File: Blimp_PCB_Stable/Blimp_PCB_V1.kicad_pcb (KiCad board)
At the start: 2 copper layers, 109.9 x 62 mm, 26 parts, among them J1 S8B-PH-K-S, J2 S4B-XH-A

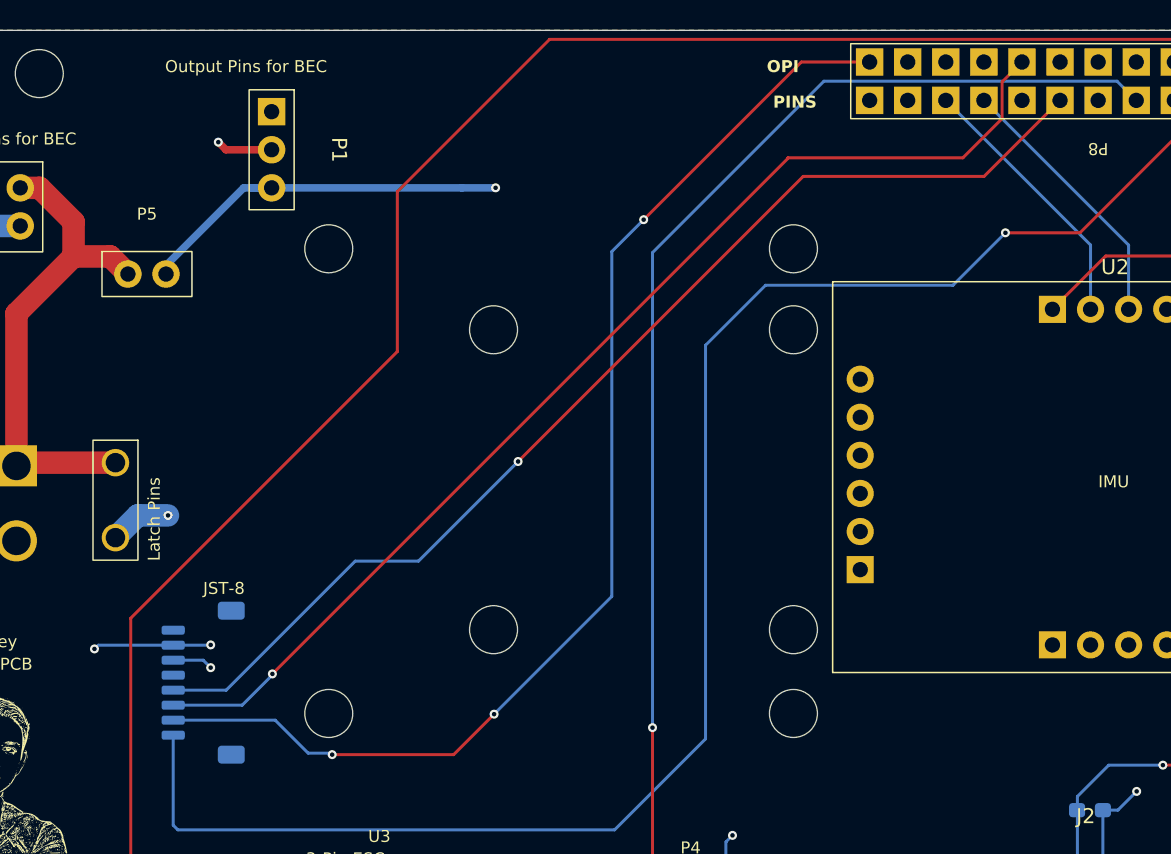
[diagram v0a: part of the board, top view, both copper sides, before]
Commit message: flip connector
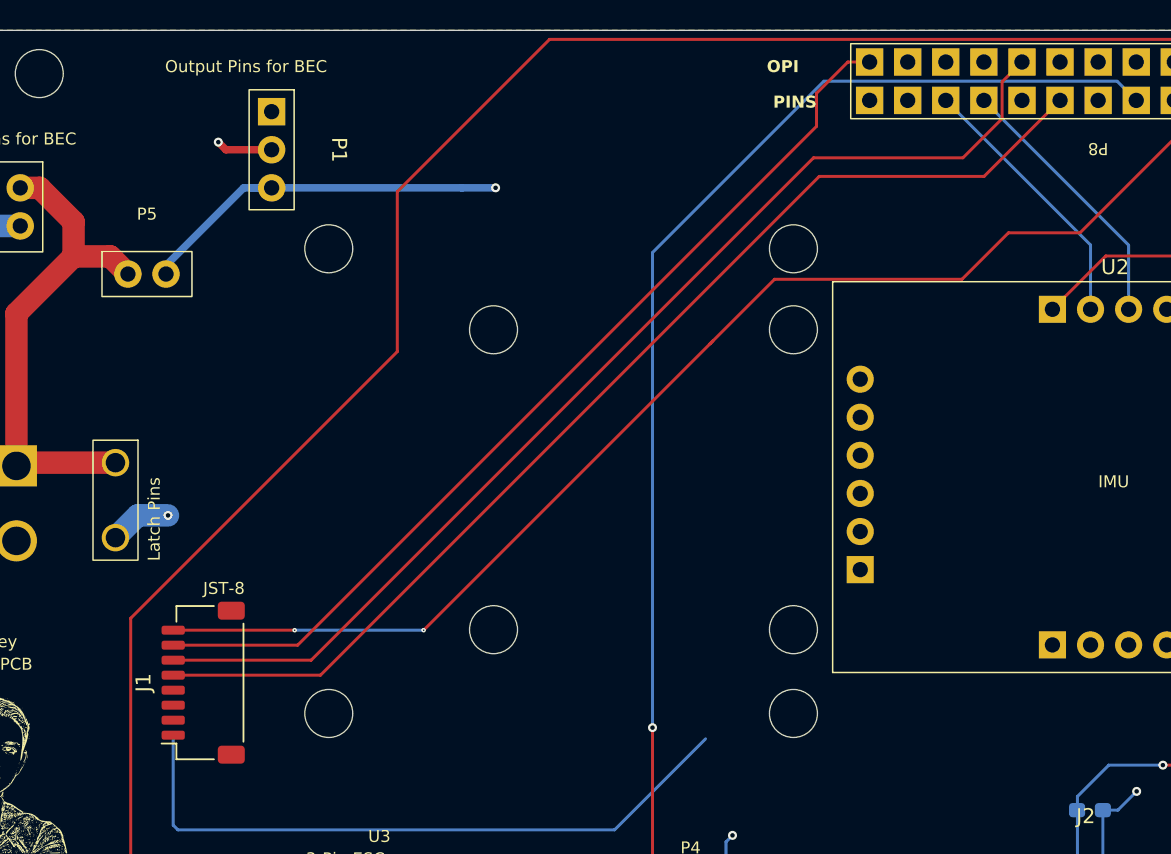
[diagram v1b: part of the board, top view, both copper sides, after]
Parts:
- J1: moved to F.Cu
- turned J1 to 90 degrees
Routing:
- net Net-(P8-PWM15): track 111.0 -> 128.4 mm, vias 1 -> 2
- net Net-(P8-PWM1): track 80.0 -> 63.9 mm, vias 3 -> 0
- net GND: track 71.4 -> 60.8 mm, vias 11 -> 8
- net Net-(P8-SCL.1): track 75.9 -> 74.6 mm, vias 1 -> 0
- net Net-(P8-CAN2_RX): track 75.4 -> 75.0 mm, vias 1 -> 0

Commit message: flip again
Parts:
- J1: moved to B.Cu
- turned J1 to -90 degrees
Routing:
- net Net-(P8-PWM15): track 128.4 -> 87.4 mm, vias 2 -> 1
- net Net-(P8-SDA.5): track 138.3 -> 127.3 mm
- net GND: track 60.8 -> 65.8 mm, vias 8 -> 10
- net Net-(P8-PWM1): track 63.9 -> 67.3 mm, vias 0 -> 3
- net Net-(P4-PWM): track 81.7 -> 85.2 mm
- net Net-(P8-SCL.1): track 74.6 -> 77.7 mm, vias 0 -> 1
- net Net-(P8-CAN2_RX): track 75.0 -> 75.4 mm, vias 0 -> 1

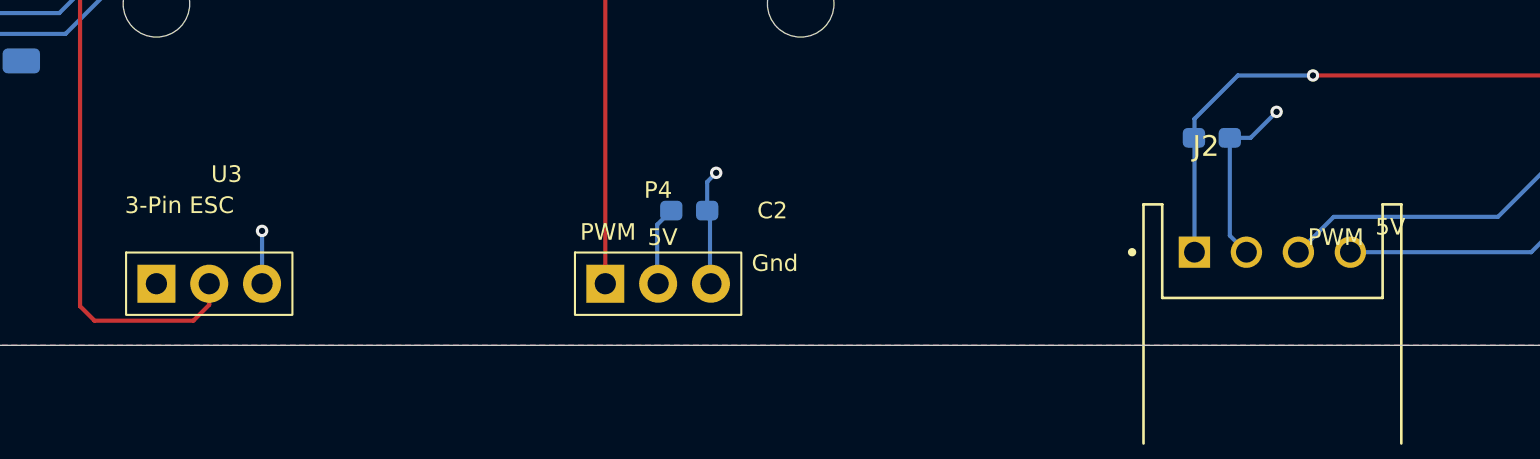
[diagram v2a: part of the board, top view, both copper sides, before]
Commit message: Cleaned some PCB silkscreen labels and fixed footprints for JST connectors
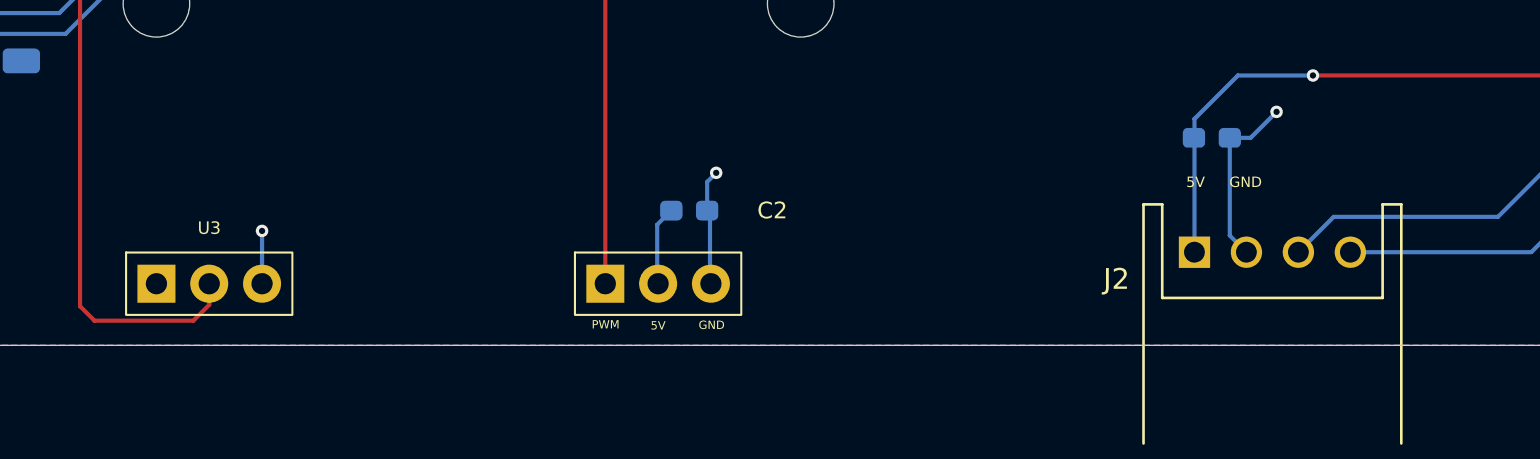
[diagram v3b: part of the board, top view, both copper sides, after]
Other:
- board text removed: "3-Pin ESC"
- board text removed: "5V"
- board text removed: "GND"
- board text removed: "PWM"

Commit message: Relabel, Fix 3D models, starting to remap not done yet
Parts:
- removed the ? at (141.7, 91.2)
- removed the ? at (165.9, 89.9)
- removed the ? at (141.2, 108.5)
- removed the ? at (165.9, 109.0)
- added R1: 30K, Capacitor_SMD:C_0603_1608Metric_Pad1.08x0.95mm_HandSolder, F.Cu at (183.4, 111.4)
- added R2: 7.5K, Capacitor_SMD:C_0603_1608Metric_Pad1.08x0.95mm_HandSolder, F.Cu at (176.1, 111.4)
- J1: footprint JST Connector:JST_SH_SM08B-SRSS-TB_1x08-1MP_P1.00mm_Horizontal -> Connector_JST:JST_SH_BM08B-SRSS-TB_1x08-1MP_P1.00mm_Vertical
- moved B1 100.9 mm to (207.4, 100.0), turned to -90 degrees
- moved P3 91.4 mm to (200.0, 112.5)
- moved U2 89.0 mm to (116.7, 44.6)
- moved P1 77.2 mm to (208.0, 83.6)
- moved P9 71.1 mm to (190.4, 114.2)
- moved P5 68.1 mm to (175.9, 127.8)
- moved C3 38.5 mm to (200.8, 85.7), turned to 90 degrees
- moved ? 15.0 mm to (149.8, 115.4)
- moved ? 15.0 mm to (180.8, 115.4)
- moved ? 15.0 mm to (149.8, 84.4)
- moved ? 15.0 mm to (180.8, 84.4)
- moved J2 6.45 mm to (195.0, 132.4)
- moved P8 1.09 mm to (186.2, 73.5)
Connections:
- P1 pad 1: unconnected-(P1-X-Pad1) -> (no net)
- P5 pad 1: BV -> Net-(P5-Pad1)
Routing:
- net Net-(P8-SDA.5): track 127.3 -> 0.00 mm
- net +5V: track 88.9 -> 0.00 mm, vias 2 -> 0
- net Net-(P8-PWM15): track 87.4 -> 0.00 mm, vias 1 -> 0
- net Net-(P4-PWM): track 85.2 -> 0.00 mm, vias 1 -> 0
- net Net-(P8-TXD.0): track 84.9 -> 0.00 mm
- net Net-(P8-RXD.0): track 78.8 -> 0.00 mm
- net Net-(P8-SCL.1): track 77.7 -> 0.00 mm, vias 1 -> 0
- net Net-(P8-CAN2_RX): track 75.4 -> 0.00 mm, vias 1 -> 0
- net Net-(P8-PWM1): track 67.3 -> 0.00 mm, vias 3 -> 0
- net GND: track 65.8 -> 0.00 mm, vias 10 -> 0
- net BV: track 33.2 -> 0.00 mm
- net +3.3V: track 26.7 -> 0.00 mm
- net Net-(P8-SPI4_RXD): track 17.9 -> 0.00 mm
- net Net-(P8-SPI4_TXD): track 17.9 -> 0.00 mm
- removed copper zone on F.Cu, net GND
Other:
- board text removed: "Gnd"
- board text removed: "IMU"
- board text removed: "Input Pins for BEC"
- board text removed: "Latch Pins"

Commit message: Added more 3D models and cleaned up labelling
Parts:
- J1: moved to F.Cu
- moved U2 11.6 mm to (125.0, 52.7)
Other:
- board text removed: "JST-8"
- board text removed: "OPI"
- board text removed: "Output Pins for BEC"
- board text removed: "PINS"
